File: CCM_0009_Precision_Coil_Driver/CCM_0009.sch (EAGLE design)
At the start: 130 parts, among them Q1 TIP29, Q2 TIP30, Q5 TIP29, Q6 TIP30, Q7 TIP29, Q8 TIP30, U1 ADA4898-2, U10 ADA4898-2, U11 AD8276, U12 AD4898-1, U13 BUF634, U14 ADA4898-2, U15 AD8276, U16 AD4898-1, U2 AD8276, U3 BUF634, U4 AD4898-1, U9 BUF634, X1 1-227161-0, X10 22-23-2021, X11 22-23-2031, X12 22-23-2031, X13 1-227161-0, X14 22-23-2021, X15 22-23-2031, X16 22-23-2031, X2 22-23-2021, X4 22-23-2031, X5 22-23-2031, X6 22-23-2031, X7 22-23-2031, X9 1-227161-0

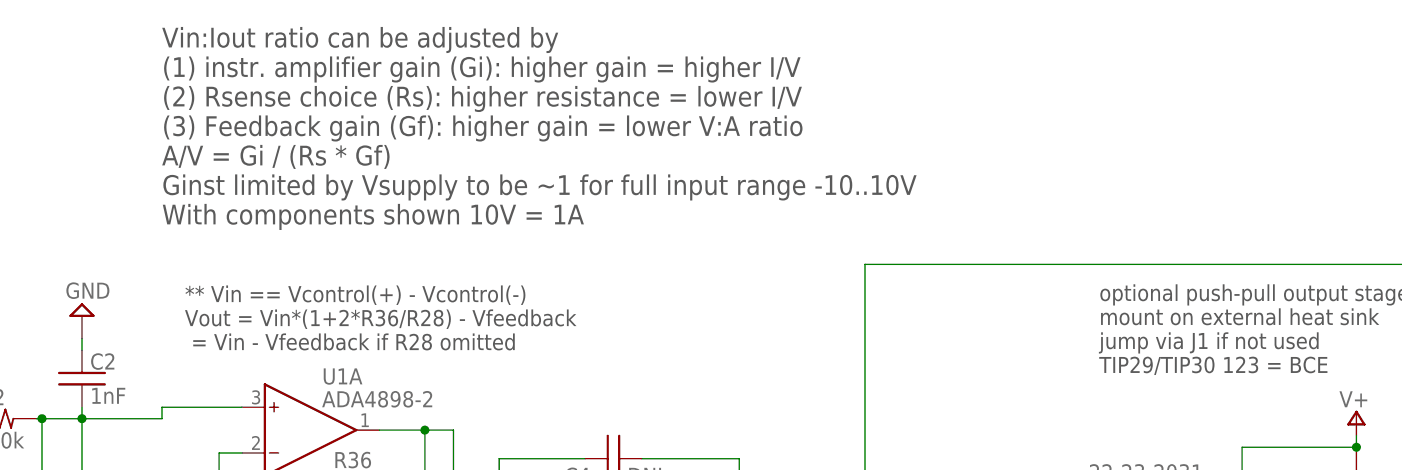
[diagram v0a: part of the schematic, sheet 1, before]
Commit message: Shutter driver added.
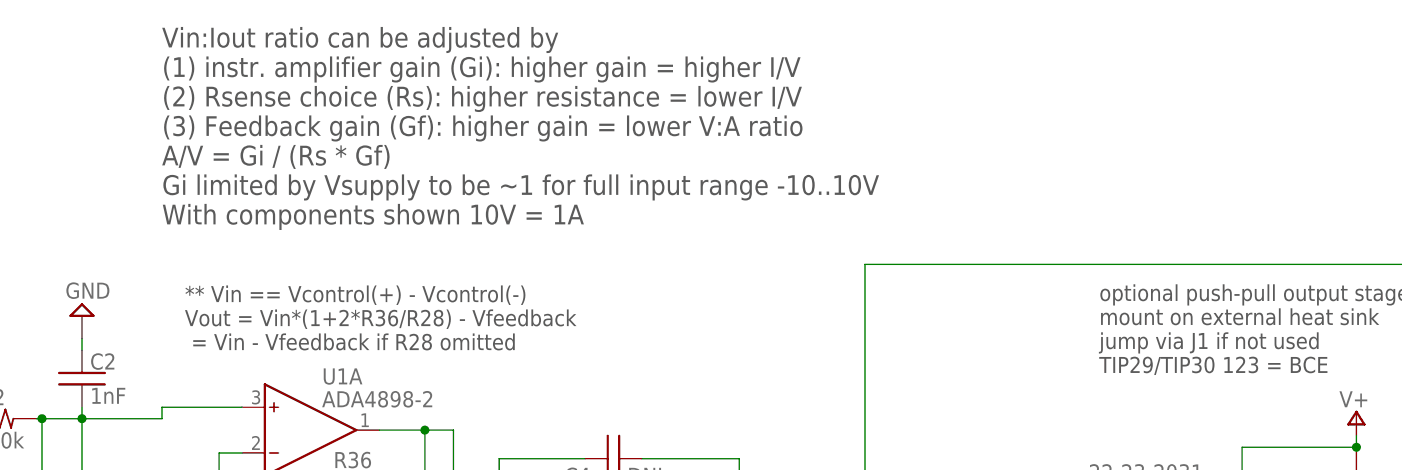
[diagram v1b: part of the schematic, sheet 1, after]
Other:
- note added: "Vin:Iout ratio can be adjusted by (1) instr. amplifier gain (Gi): higher gain = higher I/V (2) Rsense choice (Rs): higher resistance = lower I/V (3) Feedback gain (Gf): higher gain = lower V:A ratio A/V = Gi / (Rs * Gf) Gi limited by Vsupply to be ~1 for full input range -10..10V With components shown 10V = 1A"
- note removed: "Vin:Iout ratio can be adjusted by (1) instr. amplifier gain (Gi): higher gain = higher I/V (2) Rsense choice (Rs): higher resistance = lower I/V (3) Feedback gain (Gf): higher gain = lower V:A ratio A/V = Gi / (Rs * Gf) Ginst limited by Vsupply to be ~1 for full input range -10..10V With components shown 10V = 1A"
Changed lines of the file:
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@@
 <?xml version="1.0" encoding="utf-8"?>
 <!DOCTYPE eagle SYSTEM "eagle.dtd">
-<eagle version="8.3.1">
+<eagle version="9.0.1">
 <drawing>
 <settings>
@@
 <setting verticaltext="up"/>
 </settings>
-<grid distance="0.025" unitdist="inch" unit="inch" style="lines" multiple="1" display="no" altdistance="0.01" altunitdist="inch" altunit="inch"/>
+<grid distance="0.1" unitdist="inch" unit="inch" style="lines" multiple="1" display="no" altdistance="0.01" altunitdist="inch" altunit="inch"/>
 <layers>
 <layer number="1" name="Top" color="4" fill="1" visible="no" active="no"/>
@@
 (3) Feedback gain (Gf): higher gain = lower V:A ratio
 A/V = Gi / (Rs * Gf)
-Ginst limited by Vsupply to be ~1 for full input range -10..10V
+Gi limited by Vsupply to be ~1 for full input range -10..10V
 With components shown 10V = 1A</text>
 </plain>
